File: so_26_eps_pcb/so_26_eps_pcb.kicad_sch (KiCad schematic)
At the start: 84 parts, among them J1 Conn_02x12_Odd_Even, J2 Conn_01x02, SW1 SW_SPDT

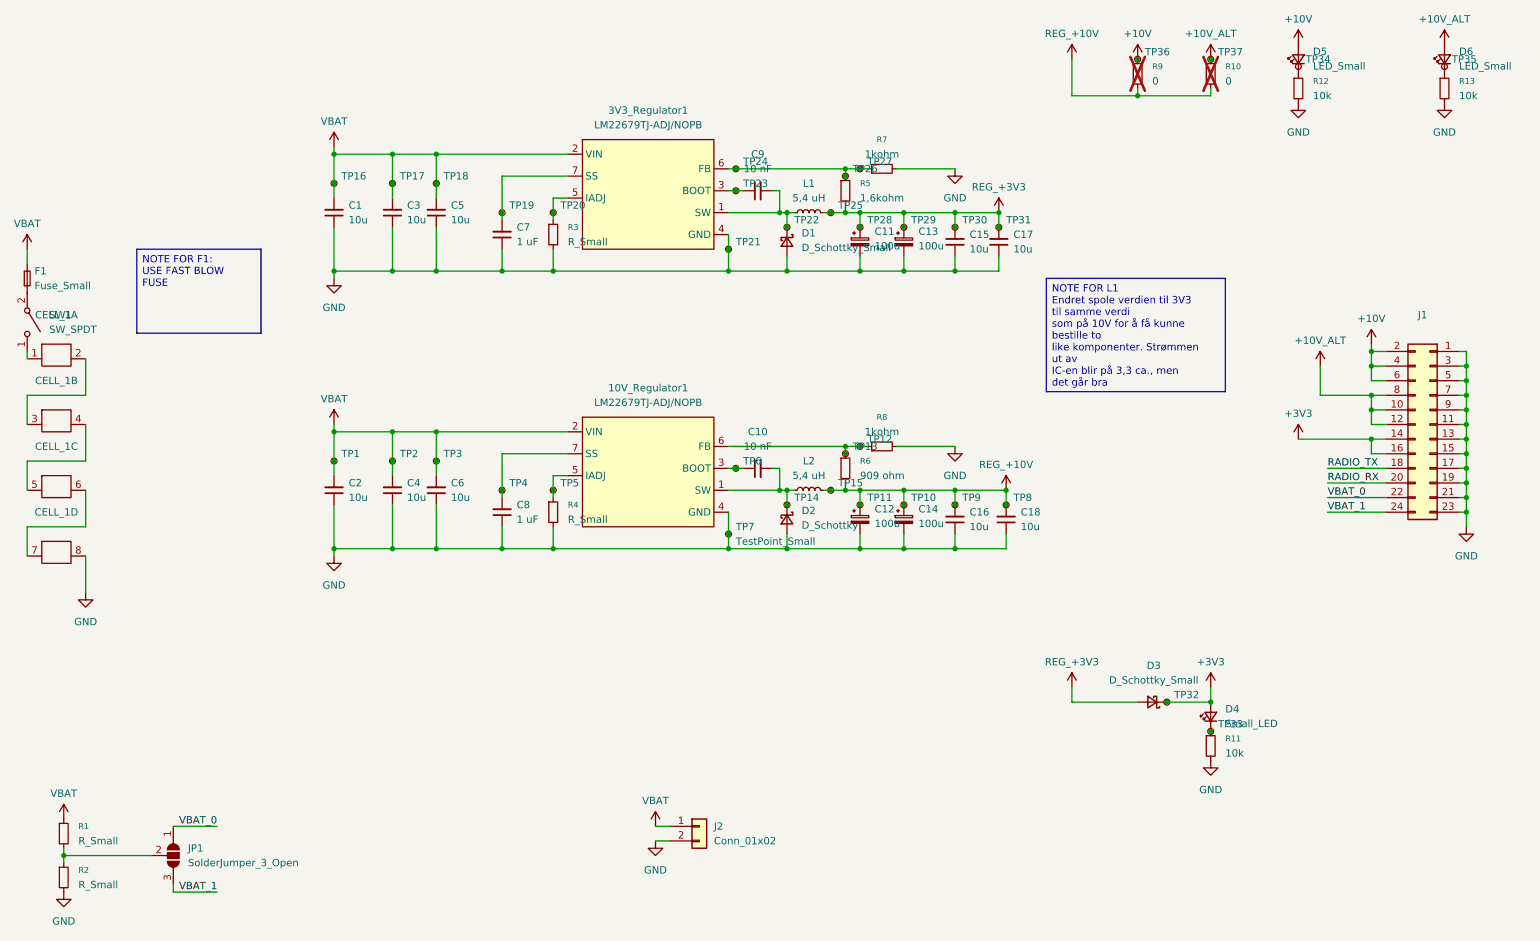
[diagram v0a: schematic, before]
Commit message: Added two headers to the system
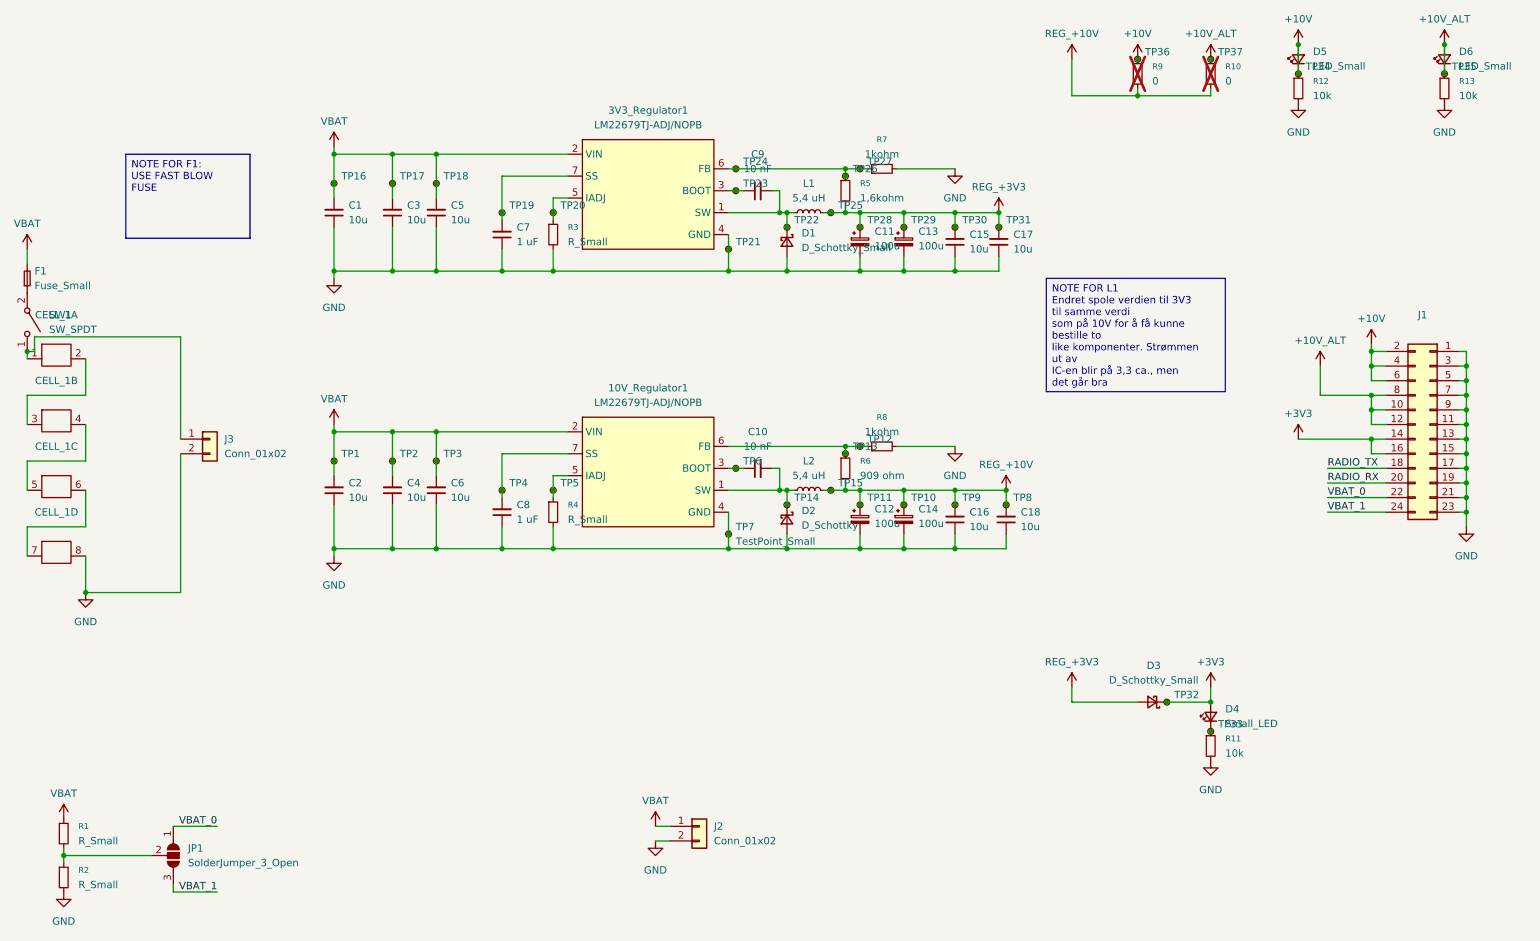
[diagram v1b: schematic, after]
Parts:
- added J3: Conn_01x02, Myfootprints:01x02_header, symbol Connector_Generic:Conn_01x02
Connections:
- net +10V: now also D5.1 (K), R12.1, TP34.1
- net +10V_ALT: now also D6.1 (K), R13.1, TP35.1
- net GND: now also J3.2 (Pin_2)
- net at CELL_1.1, SW1.1 (A): now also J3.1 (Pin_1)
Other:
- moved on the sheet: TP34, TP35
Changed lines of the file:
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@@
 	(text_box "NOTE FOR F1:\nUSE FAST BLOW FUSE"
 		(exclude_from_sim no)
-		(at 41.91 59.69 0)
+		(at 40.005 43.18 0)
 		(size 21.59 14.605)
 		(margins 0.9525 0.9525 0.9525 0.9525)
@@
 	)
 	(junction
+		(at 269.24 29.21)
+		(diameter 0)
+		(color 0 0 0 0)
+	)
+	(junction
+		(at 22.86 77.47)
+		(diameter 0)
+		(color 0 0 0 0)
+	)
+	(junction
 		(at 144.78 63.5)
 		(diameter 0)
@@
 	)
 	(junction
+		(at 243.84 29.21)
+		(diameter 0)
+		(color 0 0 0 0)
+	)
+	(junction
 		(at 93.98 43.18)
 		(diameter 0)
@@
 	)
 	(junction
+		(at 269.24 24.13)
+		(diameter 0)
+		(color 0 0 0 0)
+	)
+	(junction
 		(at 93.98 111.76)
 		(diameter 0)
@@
 	)
 	(junction
+		(at 243.84 24.13)
+		(diameter 0)
+		(color 0 0 0 0)
+	)
+	(junction
 		(at 162.56 101.6)
 		(diameter 0)
@@
 	)
 	(junction
+		(at 33.02 119.38)
+		(diameter 0)
+		(color 0 0 0 0)
+	)
+	(junction
 		(at 146.05 45.72)
 		(diameter 0)
@@
 	(wire
 		(pts
+			(xy 24.13 77.47) (xy 22.86 77.47)
+		)
+		(stroke
+			(width 0)
+			(type default)
+		)
+	)
+	(wire
+		(pts
 			(xy 154.94 101.6) (xy 154.94 104.14)
 		)
@@
 	(wire
 		(pts
+			(xy 49.53 74.93) (xy 24.13 74.93)
+		)
+		(stroke
+			(width 0)
+			(type default)
+		)
+	)
+	(wire
+		(pts
+			(xy 49.53 74.93) (xy 49.53 92.71)
+		)
+		(stroke
+			(width 0)
+			(type default)
+		)
+	)
+	(wire
+		(pts
 			(xy 165.1 53.34) (xy 167.64 53.34)
 		)
@@
 	(wire
 		(pts
+			(xy 49.53 95.25) (xy 49.53 119.38)
+		)
+		(stroke
+			(width 0)
+			(type default)
+		)
+	)
+	(wire
+		(pts
 			(xy 273.05 77.47) (xy 273.05 80.01)
 		)
@@
 	(wire
 		(pts
+			(xy 24.13 74.93) (xy 24.13 77.47)
+		)
+		(stroke
+			(width 0)
+			(type default)
+		)
+	)
+	(wire
+		(pts
 			(xy 273.05 102.87) (xy 273.05 105.41)
 		)
@@
 	(wire
 		(pts
+			(xy 49.53 119.38) (xy 33.02 119.38)
+		)
+		(stroke
+			(width 0)
+			(type default)
+		)
+	)
+	(wire
+		(pts
 			(xy 132.08 162.56) (xy 134.62 162.56)
 		)
@@
 	(wire
 		(pts
+			(xy 243.84 29.21) (xy 243.84 24.13)
+		)
+		(stroke
+			(width 0)
+			(type default)
+		)
+	)
+	(wire
+		(pts
 			(xy 167.64 109.22) (xy 167.64 111.76)
 		)
@@
 	(wire
 		(pts
+			(xy 269.24 29.21) (xy 269.24 24.13)
+		)
+		(stroke
+			(width 0)
+			(type default)
+		)
+	)
+	(wire
+		(pts
 			(xy 215.9 31.75) (xy 215.9 33.02)
 		)
@@
 	(symbol
 		(lib_id "Connector:TestPoint_Small")
-		(at 269.24 27.94 0)
+		(at 269.24 29.21 0)
 		(unit 1)
 		(exclude_from_sim no)
@@
 		(fields_autoplaced yes)
 		(property "Reference" "TP35"
-			(at 270.51 26.6699 0)
+			(at 270.51 27.9399 0)
 			(effects
 				(font
@@
 		)
 		(property "Value" "~"
-			(at 270.51 29.2099 0)
+			(at 270.51 30.4799 0)
 			(effects
 				(font
@@
 		)
 		(property "Footprint" "TestPoint:TestPoint_Pad_D1.5mm"
-			(at 274.32 27.94 0)
+			(at 274.32 29.21 0)
 			(effects
 				(font
@@
 		)
 		(property "Datasheet" "~"
-			(at 274.32 27.94 0)
+			(at 274.32 29.21 0)
 			(effects
 				(font
@@
 		)
 		(property "Description" "test point"
-			(at 269.24 27.94 0)
+			(at 269.24 29.21 0)
 			(effects
 				(font
@@
 	)
 	(symbol
+		(lib_id "Connector_Generic:Conn_01x02")
+		(at 54.61 92.71 0)
+		(unit 1)
+		(exclude_from_sim no)
+		(in_bom yes)
+		(on_board yes)
+		(dnp no)
+		(fields_autoplaced yes)
+		(property "Reference" "J3"
+			(at 57.15 92.7099 0)
+			(effects
+				(font
+					(size 1.27 1.27)
+				)
+				(justify left)
+			)
+		)
+		(property "Value" "Conn_01x02"
+			(at 57.15 95.2499 0)
+			(effects
+				(font
+					(size 1.27 1.27)
+				)
+				(justify left)
+			)
+		)
+		(property "Footprint" "Myfootprints:01x02_header"
+			(at 54.61 92.71 0)
+			(effects
+				(font
+					(size 1.27 1.27)
+				)
+				(hide yes)
+			)
+		)
+		(property "Datasheet" "~"
+			(at 54.61 92.71 0)
+			(effects
+				(font
+					(size 1.27 1.27)
+				)
+				(hide yes)
+			)
+		)
+		(property "Description" "Generic connector, single row, 01x02, script generated (kicad-library-utils/schlib/autogen/connector/)"
+			(at 54.61 92.71 0)
+			(effects
+				(font
+					(size 1.27 1.27)
+				)
+				(hide yes)
+			)
+		)
+		(pin "1"
+		)
+		(pin "2"
+		)
+		(instances
+			(project "so_26_eps_pcb"
+				(path "/bf42000f-dc59-47af-ab4a-8f583481d44f"
+					(reference "J3")
+					(unit 1)
+				)
+			)
+		)
+	)
+	(symbol
 		(lib_id "Connector:TestPoint_Small")
 		(at 93.98 48.26 0)
@@
 	(symbol
 		(lib_id "Connector:TestPoint_Small")
-		(at 243.84 27.94 0)
+		(at 243.84 29.21 0)
 		(unit 1)
 		(exclude_from_sim no)
@@
 		(fields_autoplaced yes)
 		(property "Reference" "TP34"
-			(at 245.11 26.6699 0)
+			(at 245.11 27.9399 0)
 			(effects
 				(font
@@
 		)
 		(property "Value" "~"
-			(at 245.11 29.2099 0)
+			(at 245.11 30.4799 0)
 			(effects
 				(font
@@
 		)
 		(property "Footprint" "TestPoint:TestPoint_Pad_D1.5mm"
-			(at 248.92 27.94 0)
+			(at 248.92 29.21 0)
 			(effects
 				(font
@@
 		)
 		(property "Datasheet" "~"
-			(at 248.92 27.94 0)
+			(at 248.92 29.21 0)
 			(effects
 				(font
@@
 		)
 		(property "Description" "test point"
-			(at 243.84 27.94 0)
+			(at 243.84 29.21 0)
 			(effects
 				(font

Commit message: Saved
some changes needs to be done on the wires
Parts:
- removed J2: Conn_01x02, Myfootprints:01x02_header, symbol Connector_Generic:Conn_01x02
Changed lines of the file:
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@@
 	(wire
 		(pts
-			(xy 132.08 162.56) (xy 134.62 162.56)
-		)
-		(stroke
-			(width 0)
-			(type default)
-		)
-	)
-	(wire
-		(pts
 			(xy 33.02 107.95) (xy 22.86 107.95)
 		)
@@
 	(wire
 		(pts
-			(xy 132.08 160.02) (xy 134.62 160.02)
-		)
-		(stroke
-			(width 0)
-			(type default)
-		)
-	)
-	(wire
-		(pts
 			(xy 114.3 50.8) (xy 116.84 50.8)
 		)
@@
 	)
 	(symbol
-		(lib_id "Connector_Generic:Conn_01x02")
-		(at 139.7 160.02 0)
-		(unit 1)
-		(exclude_from_sim no)
-		(in_bom yes)
-		(on_board yes)
-		(dnp no)
-		(fields_autoplaced yes)
-		(property "Reference" "J2"
-			(at 142.24 160.0199 0)
-			(effects
-				(font
-					(size 1.27 1.27)
-				)
-				(justify left)
-			)
-		)
-		(property "Value" "Conn_01x02"
-			(at 142.24 162.5599 0)
-			(effects
-				(font
-					(size 1.27 1.27)
-				)
-				(justify left)
-			)
-		)
-		(property "Footprint" "Myfootprints:01x02_header"
-			(at 139.7 160.02 0)
-			(effects
-				(font
-					(size 1.27 1.27)
-				)
-				(hide yes)
-			)
-		)
-		(property "Datasheet" "~"
-			(at 139.7 160.02 0)
-			(effects
-				(font
-					(size 1.27 1.27)
-				)
-				(hide yes)
-			)
-		)
-		(property "Description" "Generic connector, single row, 01x02, script generated (kicad-library-utils/schlib/autogen/connector/)"
-			(at 139.7 160.02 0)
-			(effects
-				(font
-					(size 1.27 1.27)
-				)
-				(hide yes)
-			)
-		)
-		(pin "1"
-		)
-		(pin "2"
-		)
-		(instances
-			(project ""
-				(path "/bf42000f-dc59-47af-ab4a-8f583481d44f"
-					(reference "J2")
-					(unit 1)
-				)
-			)
-		)
-	)
-	(symbol
 		(lib_id "Device:C_Small")
 		(at 76.2 53.34 180)
@@
 	)
 	(symbol
-		(lib_id "power:GND")
-		(at 132.08 162.56 0)
-		(unit 1)
-		(exclude_from_sim no)
-		(in_bom yes)
-		(on_board yes)
-		(dnp no)
-		(fields_autoplaced yes)
-		(property "Reference" "#PWR028"
-			(at 132.08 168.91 0)
-			(effects
-				(font
-					(size 1.27 1.27)
-				)
-				(hide yes)
-			)
-		)
-		(property "Value" "GND"
-			(at 132.08 167.64 0)
-			(effects
-				(font
-					(size 1.27 1.27)
-				)
-			)
-		)
-		(property "Footprint" ""
-			(at 132.08 162.56 0)
-			(effects
-				(font
-					(size 1.27 1.27)
-				)
-				(hide yes)
-			)
-		)
-		(property "Datasheet" ""
-			(at 132.08 162.56 0)
-			(effects
-				(font
-					(size 1.27 1.27)
-				)
-				(hide yes)
-			)
-		)
-		(property "Description" "Power symbol creates a global label with name \"GND\" , ground"
-			(at 132.08 162.56 0)
-			(effects
-				(font
-					(size 1.27 1.27)
-				)
-				(hide yes)
-			)
-		)
-		(pin "1"
-		)
-		(instances
-			(project ""
-				(path "/bf42000f-dc59-47af-ab4a-8f583481d44f"
-					(reference "#PWR028")
-					(unit 1)
-				)
-			)
-		)
-	)
-	(symbol
 		(lib_id "power:+12V")
 		(at 247.65 80.01 0)
@@
 					(unit 1)
 				)
-			)
-		)
-	)
-	(symbol
-		(lib_id "power:+12V")
-		(at 132.08 160.02 0)
-		(unit 1)
-		(exclude_from_sim no)
-		(in_bom yes)
-		(on_board yes)
-		(dnp no)
-		(property "Reference" "#PWR027"
-			(at 132.08 163.83 0)
-			(effects
-				(font
-					(size 1.27 1.27)
-				)
-				(hide yes)
-			)
-		)
-		(property "Value" "VBAT"
-			(at 132.08 155.575 0)
-			(effects
-				(font
-					(size 1.27 1.27)
-				)
-			)
-		)
-		(property "Footprint" ""
-			(at 132.08 160.02 0)
-			(effects
-				(font
-					(size 1.27 1.27)
-				)
-				(hide yes)
-			)
-		)
-		(property "Datasheet" ""
-			(at 132.08 160.02 0)
-			(effects
-				(font
-					(size 1.27 1.27)
-				)
-				(hide yes)
-			)
-		)
-		(property "Description" ""
-			(at 132.08 160.02 0)
-			(effects
-				(font
-					(size 1.27 1.27)
-				)
-			)
-		)
-		(pin "1"
-		)
-		(instances
-			(project "so_26_eps_pcb"
-				(path "/bf42000f-dc59-47af-ab4a-8f583481d44f"
-					(reference "#PWR027")
-					(unit 1)
-				)

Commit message: REV 1 FINAL
SHEMATIC AND PCB CHECK
DRC/ERC PASSED
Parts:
- removed TP1, TP10, TP11, TP12, TP13, TP14, TP15, TP16, TP17, TP18, TP19, TP2, TP20, TP21, TP22, TP23, TP24, TP25, TP26, TP27, TP28, TP29, TP3, TP30, TP31, TP32, TP33, TP34, TP35, TP36, TP37, TP4, TP5, TP6, TP8, TP9: ~, TestPoint:TestPoint_Pad_D1.5mm, symbol Connector:TestPoint_Small
- removed TP7: TestPoint_Small, TestPoint:TestPoint_Pad_D1.5mm, symbol Connector:TestPoint_Small
- renumbered 3V3_Regulator1 to U1, 10V_Regulator1 to U2
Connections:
- net +10V: no longer D5.1 (K), R12.1
- net +10V_ALT: no longer D6.1 (K), R13.1
- new net: D5.1 (K), R12.1
- new net: D6.1 (K), R13.1
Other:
- title: so_26_eps_pcb -> SO26 - EPS

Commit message: added text
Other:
- moved on the sheet: CELL_1A, CELL_1B, CELL_1C, CELL_1D, F1, SW1

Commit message: Uptaded switch footprints
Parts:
- SW1: footprint Connector_PinSocket_2.54mm:PinSocket_1x02_P2.54mm_Vertical -> Myfootprints:finalswitchfinal
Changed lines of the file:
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@@
 			)
 		)
-		(property "Footprint" "Connector_PinSocket_2.54mm:PinSocket_1x02_P2.54mm_Vertical"
+		(property "Footprint" "Myfootprints:finalswitchfinal"
 			(at 22.86 69.85 0)
 			(effects
